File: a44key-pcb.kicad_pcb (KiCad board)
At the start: 2 copper layers, 116.6 x 105.5 mm, 64 parts, among them J1 AudioJack3, J2 Conn_01x04_Female, J3 Conn_01x04_Female, SW1 SW_Push, U1 ATmega32U4-AU, Y1 16MHz

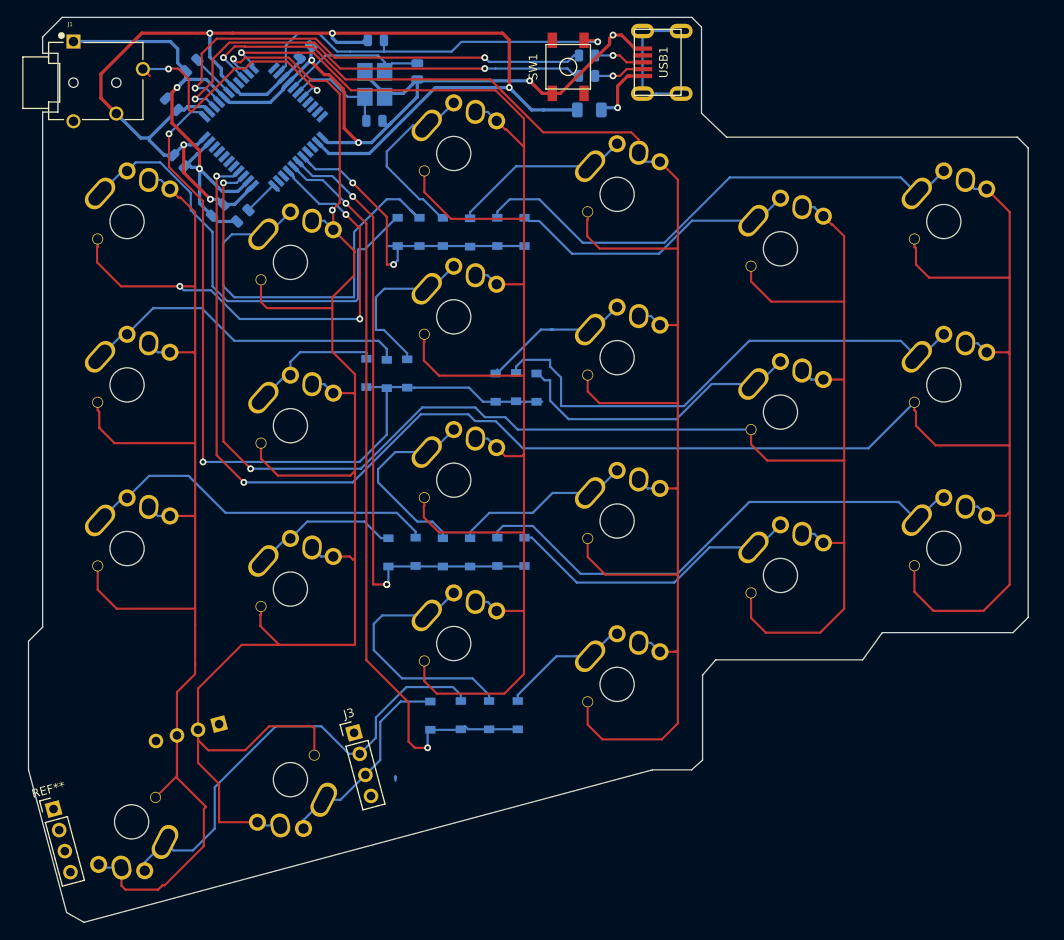
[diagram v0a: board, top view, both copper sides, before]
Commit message: Rerouting
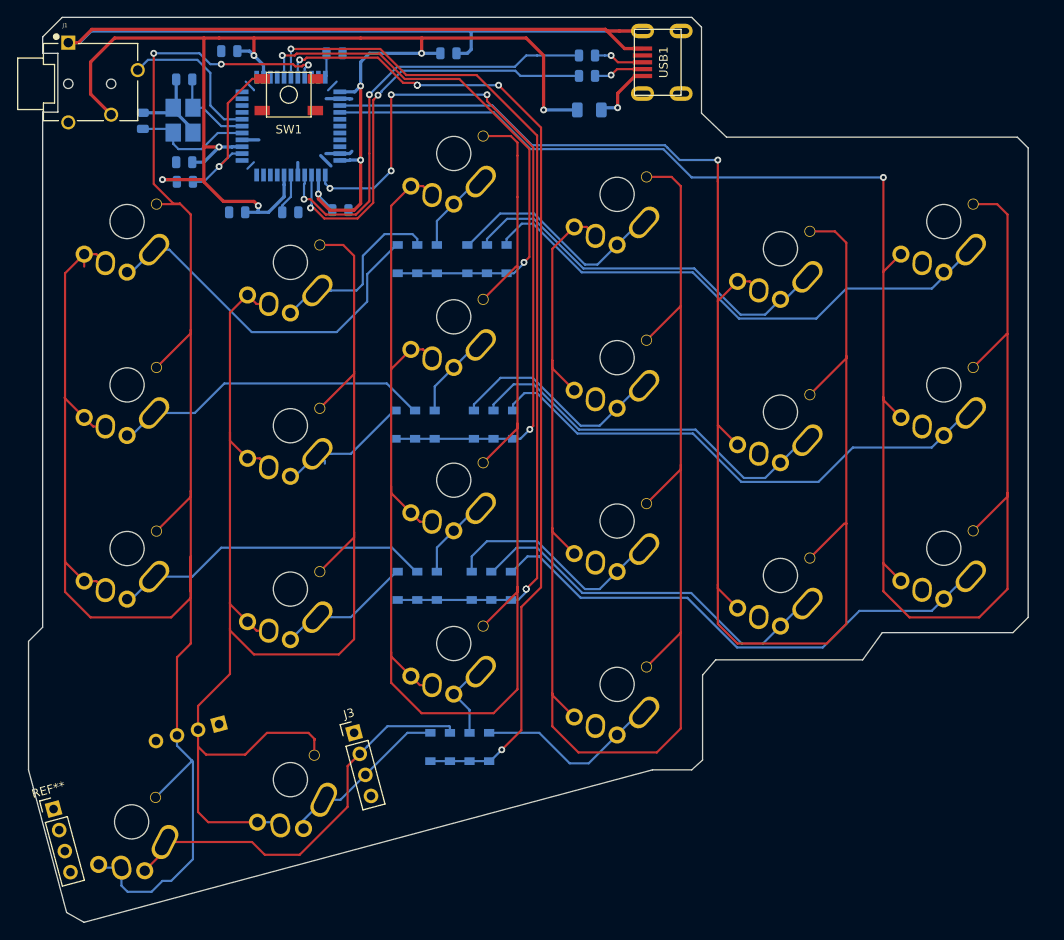
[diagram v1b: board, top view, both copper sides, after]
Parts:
- added C8: 0.1uF, Capacitor_SMD:C_0805_2012Metric, B.Cu at (119.8, 68.8)
- moved C7 32.8 mm to (132.4, 50.5), turned to 0 degrees
- moved SW1 32.7 mm to (113.8, 55.4), turned to 0 degrees
- moved C3 32.5 mm to (96.8, 58.4), turned to 90 degrees
- moved R3 27.7 mm to (101.7, 65.5)
- moved Y1 22.7 mm to (101.5, 58.3), turned to 270 degrees
- moved C2 22.7 mm to (101.6, 53.6), turned to 180 degrees
- moved R4 21.8 mm to (119.1, 50.5), turned to 180 degrees
- moved C6 20.6 mm to (114.0, 69.1), turned to 0 degrees
- moved C4 8.87 mm to (106.9, 50.3), turned to 180 degrees
- moved D6 6.92 mm to (126.2, 93.9)
- moved D10 6.77 mm to (130.8, 93.9)
- moved D2 6.77 mm to (128.5, 93.9)
- moved D18 6.62 mm to (137.7, 93.9)
- moved D19 5.54 mm to (137.4, 112.6)
- moved D17 5.41 mm to (136.9, 74.5)
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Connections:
- J2 pad 1: Net-(J2-Pad1) -> GND
- J2 pad 4: Net-(J2-Pad4) -> GND
- J3 pad 1: Net-(J3-Pad1) -> GND
- J3 pad 4: Net-(J3-Pad4) -> GND
- USB1 pad 6: Net-(USB1-Pad6) -> GND
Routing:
- net COL0: track 232.4 -> 200.7 mm, vias 2 -> 1
- net ROW2: track 74.5 -> 105.6 mm
- net ROW3: track 89.9 -> 117.5 mm, vias 2 -> 5
- net COL5: track 210.5 -> 237.2 mm
- net ROW0: track 38.5 -> 64.9 mm
- net Net-(D5-Pad2): track 49.1 -> 23.1 mm
- net Net-(R3-Pad2): track 45.8 -> 20.1 mm
- net GND: track 144.0 -> 166.9 mm, vias 6 -> 0
- net COL2: track 198.3 -> 177.1 mm, vias 1 -> 0
- net Net-(D12-Pad2): track 30.2 -> 9.52 mm
- net Net-(USB1-Pad6): track 16.3 -> 0.00 mm
- net +5V: track 155.4 -> 171.5 mm, vias 5 -> 9
- net SCL: track 31.7 -> 17.8 mm, vias 2 -> 0
- net Net-(D11-Pad2): track 22.9 -> 9.82 mm
- net Net-(D1-Pad2): track 55.2 -> 42.7 mm
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
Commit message: Rerouting
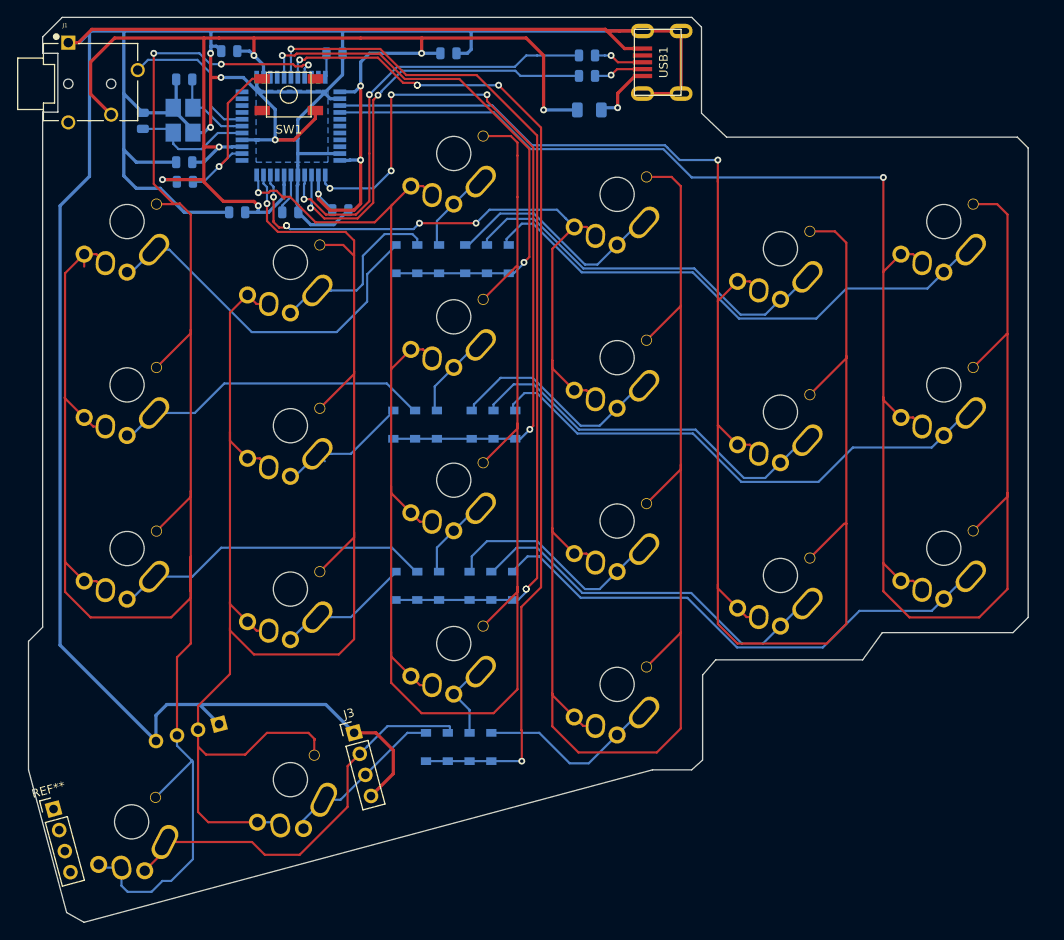
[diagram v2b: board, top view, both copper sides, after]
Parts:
- moved D8 0.51 mm to (129.8, 131.4)
- moved D11 0.25 mm to (131.3, 112.6)
- moved D14 0.25 mm to (135.1, 93.9)
- moved D22 0.25 mm to (140.0, 112.6)
- moved D9 0.25 mm to (131.3, 74.5)
- moved D1 0.25 mm to (126.2, 74.5)
- moved D6 0.25 mm to (126.0, 93.9)
- moved D7 0.25 mm to (126.2, 112.6)
- moved D10 0.25 mm to (131.1, 93.9)
- moved D13 0.25 mm to (134.4, 74.5)
- moved D15 0.25 mm to (134.9, 112.7)
- moved D16 0.25 mm to (137.4, 131.4)
- moved D20 0.25 mm to (139.4, 74.5)
- moved D21 0.25 mm to (140.2, 93.9)
- moved D4 0.25 mm to (132.3, 131.4)
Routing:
- net GND: track 166.9 -> 433.8 mm, vias 0 -> 4
- net COL2: track 177.1 -> 228.9 mm, vias 0 -> 5
- net COL3: track 185.0 -> 205.5 mm, vias 0 -> 1
- net COL4: track 184.0 -> 202.4 mm, vias 0 -> 1
- net COL0: track 200.7 -> 209.4 mm
- net COL1: track 192.4 -> 198.3 mm
- net (no net): track 3.93 -> 0.00 mm
- net ROW3: track 117.5 -> 119.3 mm
- net TH34: track 20.0 -> 19.5 mm
- added copper zone on B.Cu, net GND

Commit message: Breakout added
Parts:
- added J2: Conn_01x04_Female, Connector_PinHeader_2.54mm:PinHeader_1x04_P2.54mm_Vertical, B.Cu at (185.9, 124.5)
- added J3: Conn_01x04_Female, Connector_PinHeader_2.54mm:PinHeader_1x04_P2.54mm_Vertical, F.Cu at (200.8, 129.5)
- added MX4: MX-NoLED, MX_Alps_Hybrid:MX-Alps-Choc-X-1U-NoLED, F.Cu at (173.1, 132.8)
- added MX8: MX-NoLED, MX_Alps_Hybrid:MX-Alps-Choc-X-1U-NoLED, F.Cu at (192.2, 132.9)
- added REF**: breakaway-mousebites, random-keyboard-parts:breakaway-mousebites, F.Cu at (169.7, 121.4)
- added REF**: breakaway-mousebites, random-keyboard-parts:breakaway-mousebites, F.Cu at (169.7, 123.4)
- added REF**: breakaway-mousebites, random-keyboard-parts:breakaway-mousebites, F.Cu at (193.3, 118.4)
- added REF**: breakaway-mousebites, random-keyboard-parts:breakaway-mousebites, F.Cu at (193.3, 123.7)
- added REF**: PinHeader_1x04_P2.54mm_Vertical, Connector_PinHeader_2.54mm:PinHeader_1x04_P2.54mm_Vertical, F.Cu at (164.7, 129.1)
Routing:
- net GND: track 433.8 -> 616.1 mm, vias 4 -> 6
- net (no net): track 0.00 -> 119.2 mm
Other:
- board size 116.6 x 105.5 mm -> 118.7 x 105.5 mm

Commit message: Gerbers generated
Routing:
- net GND: track 616.1 -> 617.4 mm, vias 6 -> 7
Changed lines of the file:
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@@
     (thickness 1.6)
     (drawings 43)
-    (tracks 868)
+    (tracks 870)
     (zones 0)
     (modules 74)
@@
   (segment (start 112.202 60.64) (end 111.802001 61.039999) (width 0.381) (layer B.Cu) (net 1))
   (segment (start 111.802001 61.039999) (end 111.802001 61.256097) (width 0.381) (layer B.Cu) (net 1))
+  (segment (start 100.6625 53.594) (end 100.075 53.594) (width 0.381) (layer B.Cu) (net 1))
+  (via (at 99.314 53.594) (size 0.8) (drill 0.4) (layers F.Cu B.Cu) (net 1))
+  (segment (start 100.075 53.594) (end 99.314 53.594) (width 0.381) (layer B.Cu) (net 1))
   (segment (start 107.342 59.04) (end 108.346 59.04) (width 0.254) (layer B.Cu) (net 2))
   (segment (start 105.914 59.04) (end 107.342 59.04) (width 0.254) (layer B.Cu) (net 2))
@@
   (segment (start 95.4575 76.0675) (end 94.9325 76.0675) (width 0.254) (layer B.Cu) (net 5))
   (segment (start 98.0825 73.4425) (end 95.4575 76.0675) (width 0.254) (layer B.Cu) (net 5))
+  (segment (start 126.492 72.898) (end 126.342 72.898) (width 0.254) (layer B.Cu) (net 5))
+  (segment (start 126.342 72.898) (end 122.936 76.304) (width 0.254) (layer B.Cu) (net 5))
+  (segment (start 122.936 76.304) (end 122.936 79.502) (width 0.254) (layer B.Cu) (net 5))
+  (segment (start 122.936 79.502) (end 119.38 83.058) (width 0.254) (layer B.Cu) (net 5))
+  (segment (start 119.38 83.058) (end 109.474 83.058) (width 0.254) (layer B.Cu) (net 5))
+  (segment (start 99.8585 73.4425) (end 98.0825 73.4425) (width 0.254) (layer B.Cu) (net 5))
+  (segment (start 109.474 83.058) (end 99.8585 73.4425) (width 0.254) (layer B.Cu) (net 5))
   (segment (start 126.492 76.2) (end 139.192 76.2) (width 0.254) (layer B.Cu) (net 6))
   (segment (start 140.046 76.198) (end 141.224 75.02) (width 0.254) (layer B.Cu) (net 6))
@@
   (segment (start 138.34101 54.26701) (end 138.26499 54.26701) (width 0.254) (layer B.Cu) (net 11))
   (segment (start 128.778 54.26701) (end 138.26499 54.26701) (width 0.254) (layer B.Cu) (net 11))
-  (segment (start 118.740843 78.205) (end 117.1325 78.205) (width 0.254) (layer B.Cu) (net 12))
-  (segment (start 126.492 72.898) (end 126.342 72.898) (width 0.254) (layer B.Cu) (net 5))
-  (segment (start 126.342 72.898) (end 122.936 76.304) (width 0.254) (layer B.Cu) (net 5))
-  (segment (start 122.936 76.304) (end 122.936 79.502) (width 0.254) (layer B.Cu) (net 5))
-  (segment (start 122.936 79.502) (end 119.38 83.058) (width 0.254) (layer B.Cu) (net 5))
-  (segment (start 119.38 83.058) (end 109.474 83.058) (width 0.254) (layer B.Cu) (net 5))
-  (segment (start 99.8585 73.4425) (end 98.0825 73.4425) (width 0.254) (layer B.Cu) (net 5))
-  (segment (start 109.474 83.058) (end 99.8585 73.4425) (width 0.254) (layer B.Cu) (net 5))
   (segment (start 137.414 133.094) (end 140.968 133.094) (width 0.254) (layer B.Cu) (net 11))
   (via (at 140.968 133.094) (size 0.8) (drill 0.4) (layers F.Cu B.Cu) (net 11))
@@
   (segment (start 140.968 129.53998) (end 140.968 133.094) (width 0.254) (layer F.Cu) (net 11))
   (segment (start 140.91601 129.48799) (end 140.968 129.53998) (width 0.254) (layer F.Cu) (net 11))
+  (segment (start 118.740843 78.205) (end 117.1325 78.205) (width 0.254) (layer B.Cu) (net 12))
   (segment (start 116.6075 78.205) (end 117.1325 78.205) (width 0.254) (layer B.Cu) (net 12))
   (segment (start 113.9825 80.83) (end 116.6075 78.205) (width 0.254) (layer B.Cu) (net 12))
@@
   (segment (start 113.943923 67.280019) (end 116.923434 70.25953) (width 0.254) (layer F.Cu) (net 32))
   (segment (start 112.362961 66.582999) (end 113.059981 67.280019) (width 0.254) (layer F.Cu) (net 32))
-  (segment (start 113.059981 67.280019) (end 113.284 67.504038) (width 0.254) (layer F.Cu) (net 32))
   (segment (start 125.73 68.332499) (end 125.86025 68.20225) (width 0.254) (layer F.Cu) (net 32))
   (segment (start 113.059981 67.280019) (end 113.943923 67.280019) (width 0.254) (layer F.Cu) (net 32))

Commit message: Gerbers generated
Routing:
- net GND: track 617.4 -> 463.9 mm
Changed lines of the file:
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@@
     (thickness 1.6)
     (drawings 43)
-    (tracks 870)
+    (tracks 857)
     (zones 0)
     (modules 74)
@@
   (segment (start 159.54375 55.24375) (end 157.81275 55.24375) (width 0.381) (layer F.Cu) (net 1))
   (segment (start 124.030802 121.83115) (end 121.652662 119.45301) (width 0.508) (layer F.Cu) (net 1))
-  (segment (start 115.318556 144.583116) (end 124.030802 135.87087) (width 0.508) (layer F.Cu) (net 1))
-  (segment (start 85.570901 135.610759) (end 88.321401 138.361259) (width 0.508) (layer F.Cu) (net 1))
-  (segment (start 90.16509 145.839575) (end 91.704868 147.379353) (width 0.508) (layer F.Cu) (net 1))
-  (segment (start 88.321401 138.361259) (end 88.321401 141.763373) (width 0.508) (layer F.Cu) (net 1))
-  (segment (start 100.421156 144.59901) (end 115.259292 144.59901) (width 0.508) (layer F.Cu) (net 1))
-  (segment (start 88.321401 141.763373) (end 90.16509 143.607062) (width 0.508) (layer F.Cu) (net 1))
-  (segment (start 90.16509 143.607062) (end 90.16509 145.839575) (width 0.508) (layer F.Cu) (net 1))
-  (segment (start 85.570901 63.002021) (end 85.570901 135.610759) (width 0.508) (layer F.Cu) (net 1))
-  (segment (start 91.704868 147.379353) (end 97.640813 147.379353) (width 0.508) (layer F.Cu) (net 1))
-  (segment (start 124.030802 135.87087) (end 124.030802 121.83115) (width 0.508) (layer F.Cu) (net 1))
-  (segment (start 89.357001 59.215921) (end 85.570901 63.002021) (width 0.508) (layer F.Cu) (net 1))
-  (segment (start 97.640813 147.379353) (end 100.421156 144.59901) (width 0.508) (layer F.Cu) (net 1))
-  (segment (start 115.259292 144.59901) (end 115.318556 144.583116) (width 0.508) (layer F.Cu) (net 1))
   (segment (start 154.47625 49.99375) (end 154.432 50.038) (width 0.508) (layer F.Cu) (net 1))
   (segment (start 155.04375 49.99375) (end 154.47625 49.99375) (width 0.508) (layer F.Cu) (net 1))
   (segment (start 152.9965 50.038) (end 150.90225 47.94375) (width 0.508) (layer F.Cu) (net 1))
   (segment (start 154.432 50.038) (end 152.9965 50.038) (width 0.508) (layer F.Cu) (net 1))
-  (segment (start 88.926 49.302) (end 89.357001 49.733001) (width 0.508) (layer F.Cu) (net 1))
   (segment (start 88.078 49.302) (end 88.926 49.302) (width 0.508) (layer F.Cu) (net 1))
-  (segment (start 89.357001 49.733001) (end 89.357001 59.215921) (width 0.508) (layer F.Cu) (net 1))
   (segment (start 88.078 49.302) (end 89.411 49.302) (width 0.508) (layer F.Cu) (net 1))
   (segment (start 89.411 49.302) (end 90.76925 47.94375) (width 0.508) (layer F.Cu) (net 1))
@@
   (segment (start 89.9325 73.967499) (end 87.699999 76.2) (width 0.254) (layer F.Cu) (net 30))
   (segment (start 87.699999 109.8662) (end 89.935521 112.101722) (width 0.254) (layer F.Cu) (net 30))
-  (segment (start 89.9325 93.017499) (end 87.63 90.714999) (width 0.254) (layer F.Cu) (net 30))
   (segment (start 87.699999 109.658001) (end 87.699999 109.8662) (width 0.254) (layer F.Cu) (net 30))
-  (segment (start 87.699999 76.2) (end 87.699999 109.658001) (width 0.254) (layer F.Cu) (net 30))
   (segment (start 101.0285 68.1355) (end 98.3615 68.1355) (width 0.254) (layer F.Cu) (net 30))
   (segment (start 87.699999 113.353999) (end 90.678 116.332) (width 0.254) (layer F.Cu) (net 30))
@@
   (segment (start 104.648 51.816) (end 105.918 51.816) (width 0.254) (layer B.Cu) (net 30))
   (via (at 105.918 51.816) (size 0.8) (drill 0.4) (layers F.Cu B.Cu) (net 30))
+  (segment (start 87.699999 90.784998) (end 87.699999 90.493999) (width 0.254) (layer F.Cu) (net 30))
+  (segment (start 89.9325 93.017499) (end 87.699999 90.784998) (width 0.254) (layer F.Cu) (net 30))
+  (segment (start 87.699999 76.2) (end 87.699999 90.493999) (width 0.254) (layer F.Cu) (net 30))
+  (segment (start 87.699999 90.493999) (end 87.699999 109.658001) (width 0.254) (layer F.Cu) (net 30))
   (segment (start 112.425164 140.219612) (end 112.79881 140.593258) (width 0.254) (layer B.Cu) (net 31))
   (segment (start 110.136383 140.219612) (end 112.425164 140.219612) (width 0.254) (layer B.Cu) (net 31))

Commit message: Gerbers generated
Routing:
- net GND: track 463.9 -> 460.6 mm
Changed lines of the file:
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@@
     (thickness 1.6)
     (drawings 43)
-    (tracks 857)
+    (tracks 856)
     (zones 0)
     (modules 74)
@@
   (segment (start 157.81275 55.24375) (end 155.04375 55.24375) (width 0.381) (layer F.Cu) (net 1))
   (segment (start 159.54375 55.24375) (end 157.81275 55.24375) (width 0.381) (layer F.Cu) (net 1))
-  (segment (start 124.030802 121.83115) (end 121.652662 119.45301) (width 0.508) (layer F.Cu) (net 1))
   (segment (start 154.47625 49.99375) (end 154.432 50.038) (width 0.508) (layer F.Cu) (net 1))
   (segment (start 155.04375 49.99375) (end 154.47625 49.99375) (width 0.508) (layer F.Cu) (net 1))
